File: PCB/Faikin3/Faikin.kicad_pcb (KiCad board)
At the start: 2 copper layers, 70 x 70 mm, 28 parts, among them J1 1x5, J2 Prog, Q3 PMF250XNEX, U1 ESP32-PICO-MINI-02, U3 MD8942, U4 Barcode

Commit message: Order
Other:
- board text removed: "JLCJLCJLC"

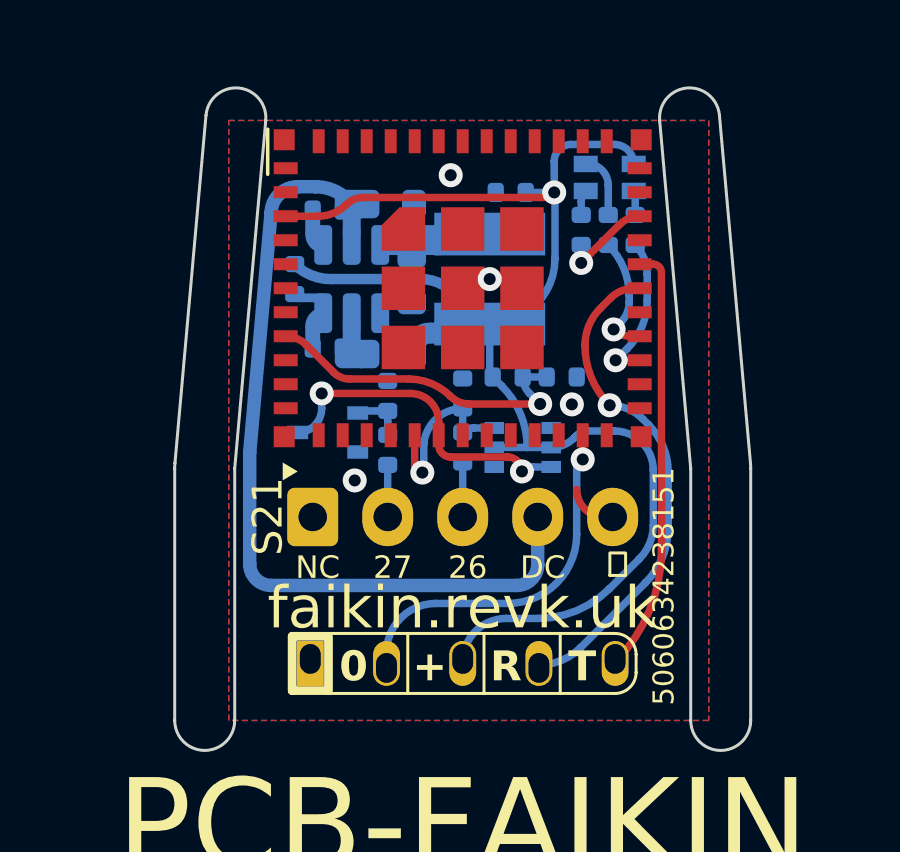
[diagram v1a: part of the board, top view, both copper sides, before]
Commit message: Changed to open collector output
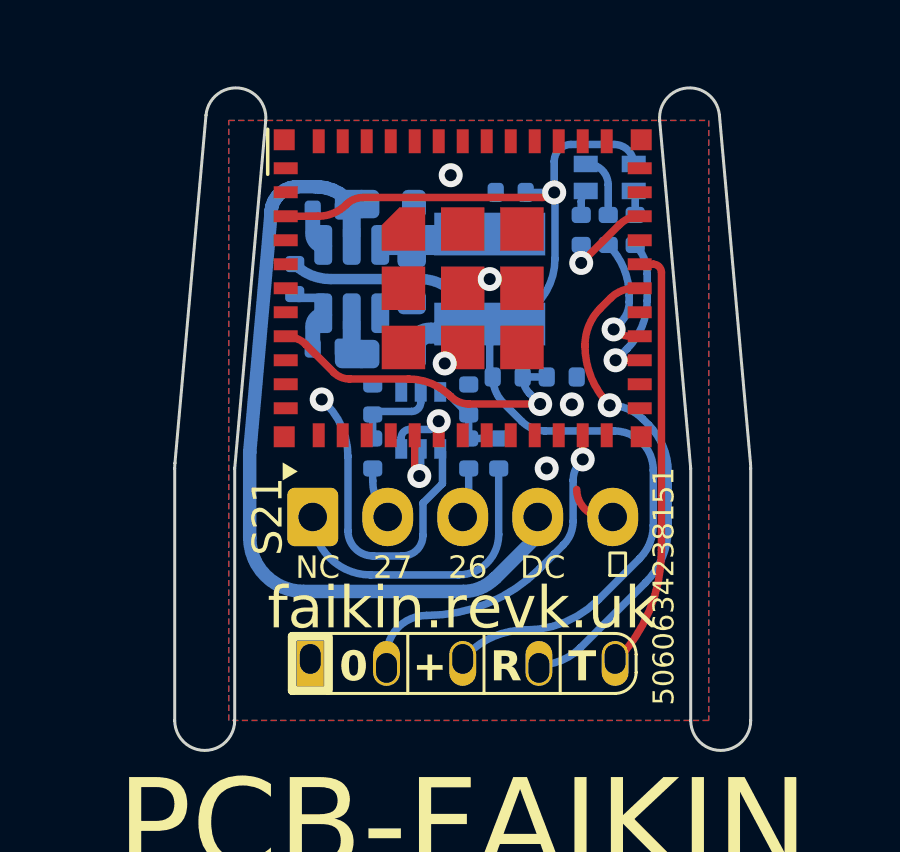
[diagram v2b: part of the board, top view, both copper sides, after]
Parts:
- removed D1: BAV99S, RevK:SOT-363_SC-70-6
- removed Q3: PMF250XNEX, RevK:SOT-323_SC-70
- removed R7: 100R, RevK:R_0402
- added Q1: BSD235C, RevK:SOT-363_SC-70-6, B.Cu at (133.6, 61.0)
- added R1: 4k7, RevK:R_0402, B.Cu at (136.2, 62.1)
- added R2: 100R, RevK:R_0402, B.Cu at (135.2, 62.1)
- R10: value 40k2 -> 39k2
- moved C7 0.51 mm to (132.0, 60.3)
- moved R8 0.51 mm to (132.0, 62.1)
- moved C6 0.28 mm to (135.2, 60.3)
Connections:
- C6 pad 2: TX -> Net-(Q1B-SP)
- J1 pad 1: unconnected-(J1-Pin_1-Pad1) -> Net-(J1-Pin_1)
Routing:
- net GND: track 1.69 -> 12.4 mm, vias 4 -> 6
- net Net-(J1-Pin_1): track 0.00 -> 10.1 mm
- net RX: track 11.2 -> 2.35 mm, vias 2 -> 1
- net TX: track 6.09 -> 2.35 mm
- net Net-(Q1B-SP): track 0.00 -> 3.04 mm
- net +3.3V: track 40.9 -> 38.5 mm
- net DC: track 26.8 -> 25.1 mm
- net Net-(Q1A-GN): track 1.64 -> 2.81 mm
- net Net-(J1-Pin_3): track 1.82 -> 1.13 mm
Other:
- board text added: "5V"

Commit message: Fix FET
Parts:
- Q1: value BSD235C -> BSS138PS
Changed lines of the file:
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@@
     (descr "SOT-363, SC-70-6")
     (tags "SOT-363 SC-70-6")
+    (property "JLCPCB Rotation Offset" "90")
+    (property "LCSC Part #" "C193381")
     (property "Sheetfile" "Faikin.kicad_sch")
     (property "Sheetname" "")
@@
         (effects (font (size 0.5 0.5) (thickness 0.08)) (justify mirror))
     )
-    (fp_text value "BSD235C" (at 0 0.05) (layer "B.Fab")
+    (fp_text value "BSS138PS" (at 0 0.05) (layer "B.Fab")
         (effects (font (size 0.5 0.5) (thickness 0.08)) (justify mirror))
     )
@@
     (fp_line (start 12.5 6.7) (end 12.5 -1.5)
       (stroke (width 0.1) (type solid)) (layer "B.Fab"))
-    (pad "1" thru_hole roundrect (at 0 0) (size 1.7 1.95) (drill 0.95) (layers "*.Cu" "*.Mask") (roundrect_rratio 0.147059)
+    (pad "1" thru_hole roundrect (at 0 0) (size 1.7 1.95) (drill 0.95) (layers "*.Cu" "*.Mask") (roundrect_rratio 0.1470588235)
       (net 45 "Net-(J1-Pin_1)") (pinfunction "Pin_1") (pintype "passive"))
     (pad "2" thru_hole oval (at 2.5 0) (size 1.7 1.95) (drill 0.95) (layers "*.Cu" "*.Mask")

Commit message: Silk tidy
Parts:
- removed U4: Barcode, RevK:EAN-5060634238151
- added C2: 100nF, RevK:C_0402, B.Cu at (138.4, 57.8)
- moved J2 0.45 mm to (135.0, 69.5)
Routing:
- net +3.3V: track 38.5 -> 40.4 mm
- net Net-(J2-0): track 11.6 -> 12.4 mm
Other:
- board text added: "12V"
- board text added: "F"
- board text added: "aikin"
- board text removed: "${TITLE}"
- board text removed: "DC"
- board text removed: "Faikin"
- board text removed: "NC"
- board text removed: "This is an assembled printed circuit board. This is a component, with no case or leads. Snap off any extra blank panels. Use this part for your own projects as you wish. Made in China for Andrews & Arnold Ltd."
- board text removed: "®"
